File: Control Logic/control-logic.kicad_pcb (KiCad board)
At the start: 2 copper layers, 90.2 x 99.1 mm, 94 parts, among them J1 Power, J2 IR, J3 Flags #2, J4 Flags #1, SW1 SW_Push, U1 74LS00, U2 74LS161, U3 74LS138, U4 24C16, U5 24C16, U6 74LS04, U7 74LS04

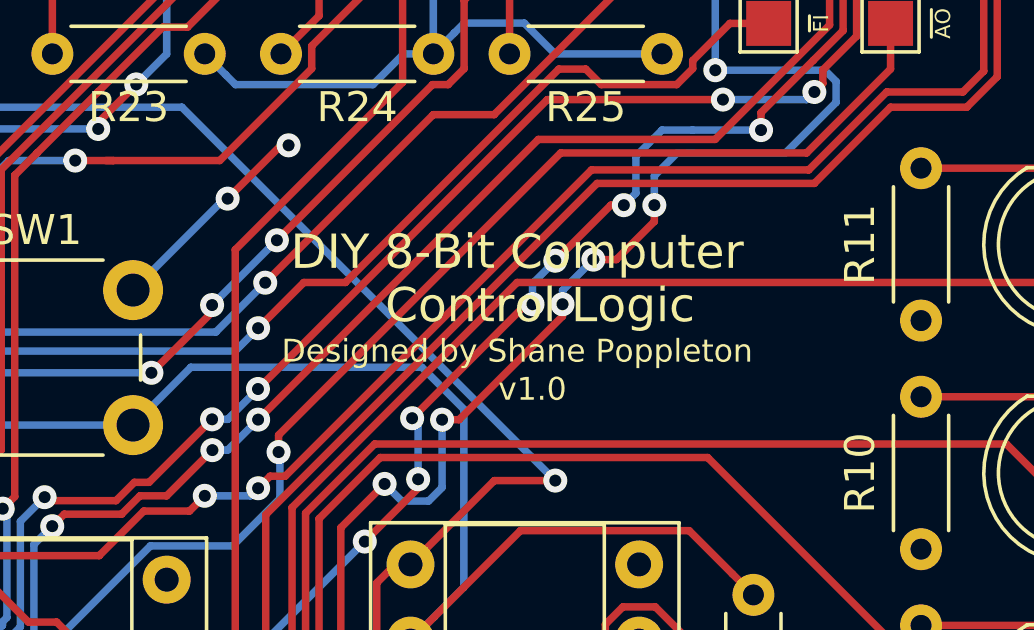
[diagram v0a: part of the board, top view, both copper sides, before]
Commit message: Added Attribution on each PCB, and regenerated gerbers
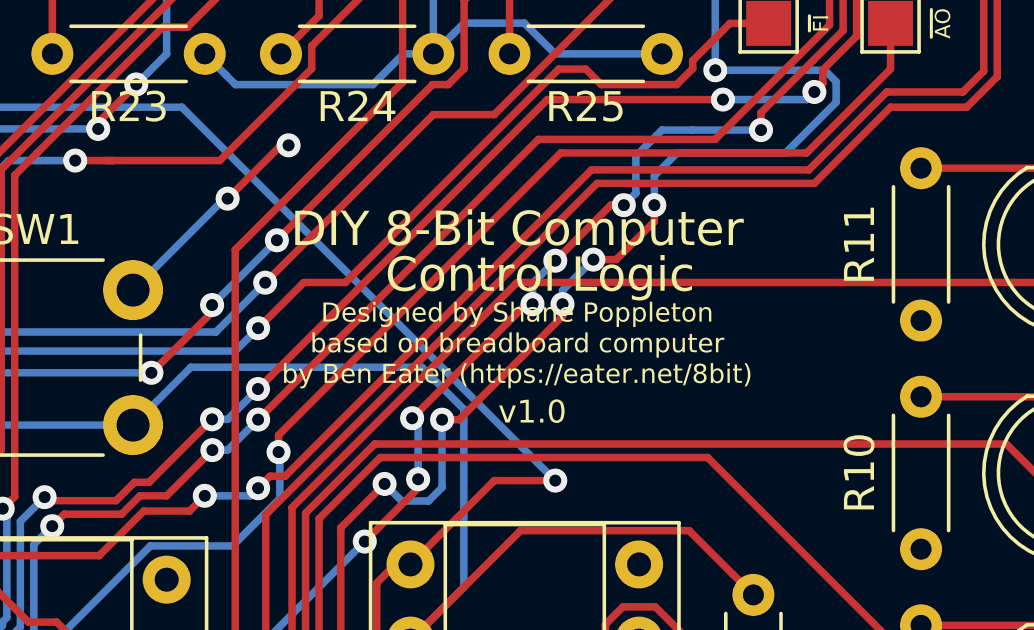
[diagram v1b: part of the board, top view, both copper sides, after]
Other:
- board text added: "Designed by Shane Poppleton based on breadboard computer by Ben Eater (https://eater.net/8bit)"
- board text removed: "Designed by Shane Poppleton"
